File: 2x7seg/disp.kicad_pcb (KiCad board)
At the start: 2 copper layers, 35.8 x 30.5 mm, 11 parts, among them P1 CONN_01X08, P2 CONN_01X08, U1 TLC59282

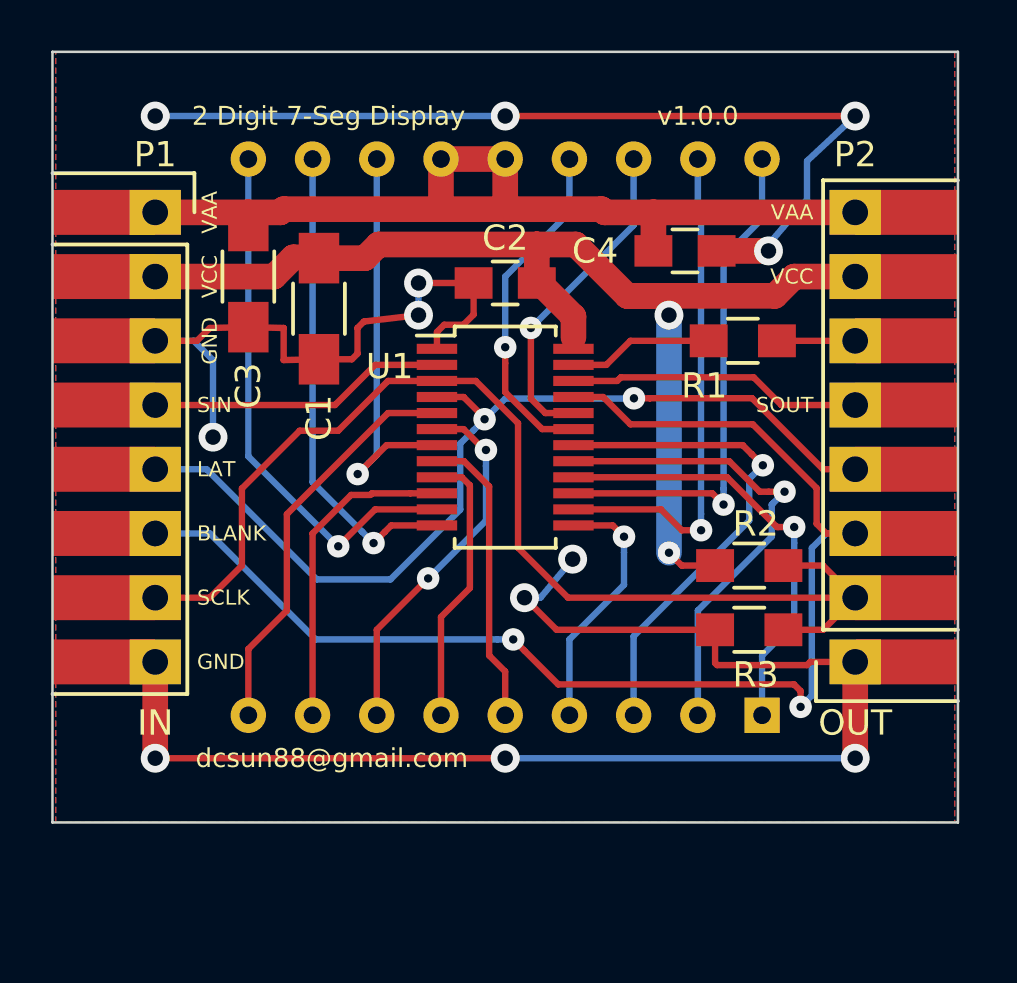
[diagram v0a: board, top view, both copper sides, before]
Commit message: Next version of display board. Increase size of holes for display pins.
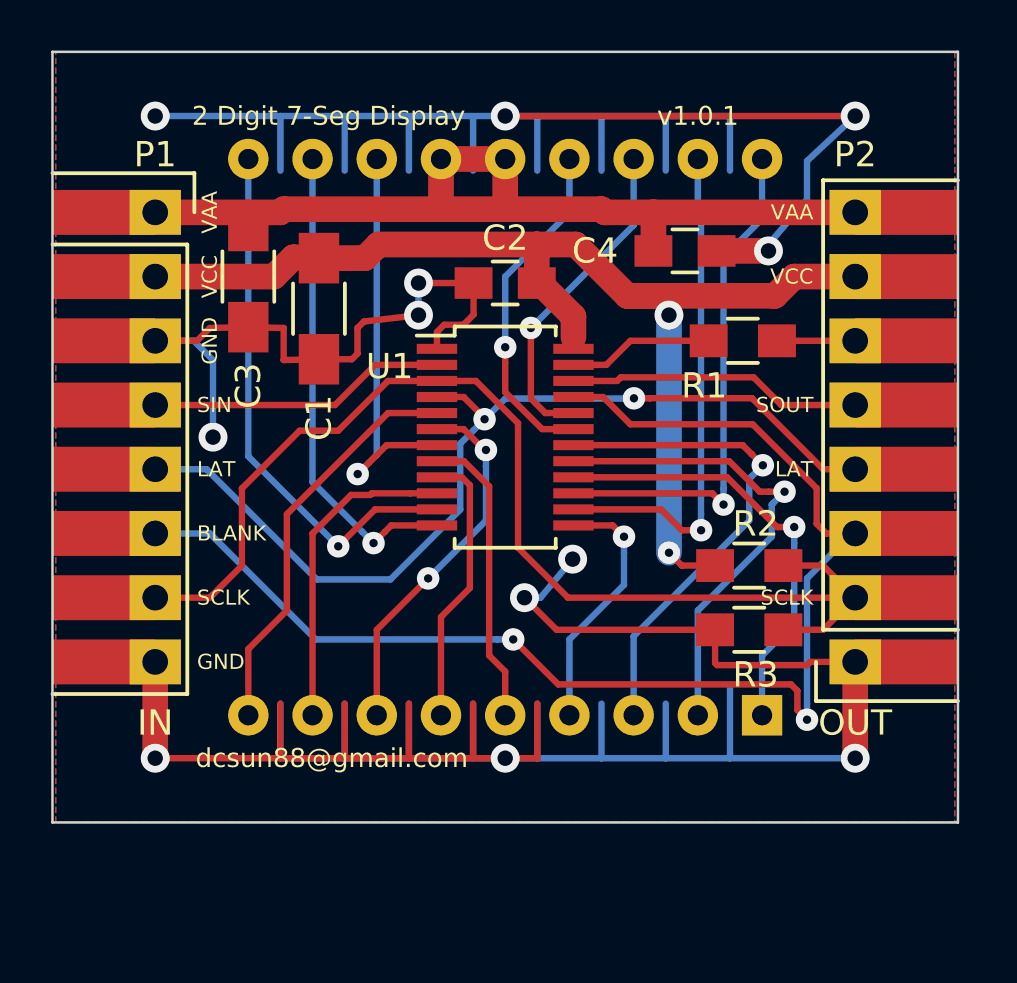
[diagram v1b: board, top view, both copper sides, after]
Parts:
- R1: value 5.05K -> 5.11K
- R2, R3: value 200 -> 249
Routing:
- net GND: track 124.6 -> 189.7 mm
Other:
- board text added: "v1.0.1"
- board text removed: "v1.0.0"

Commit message: Hide value in stitching via. Reduce width of display board by 10 mils.
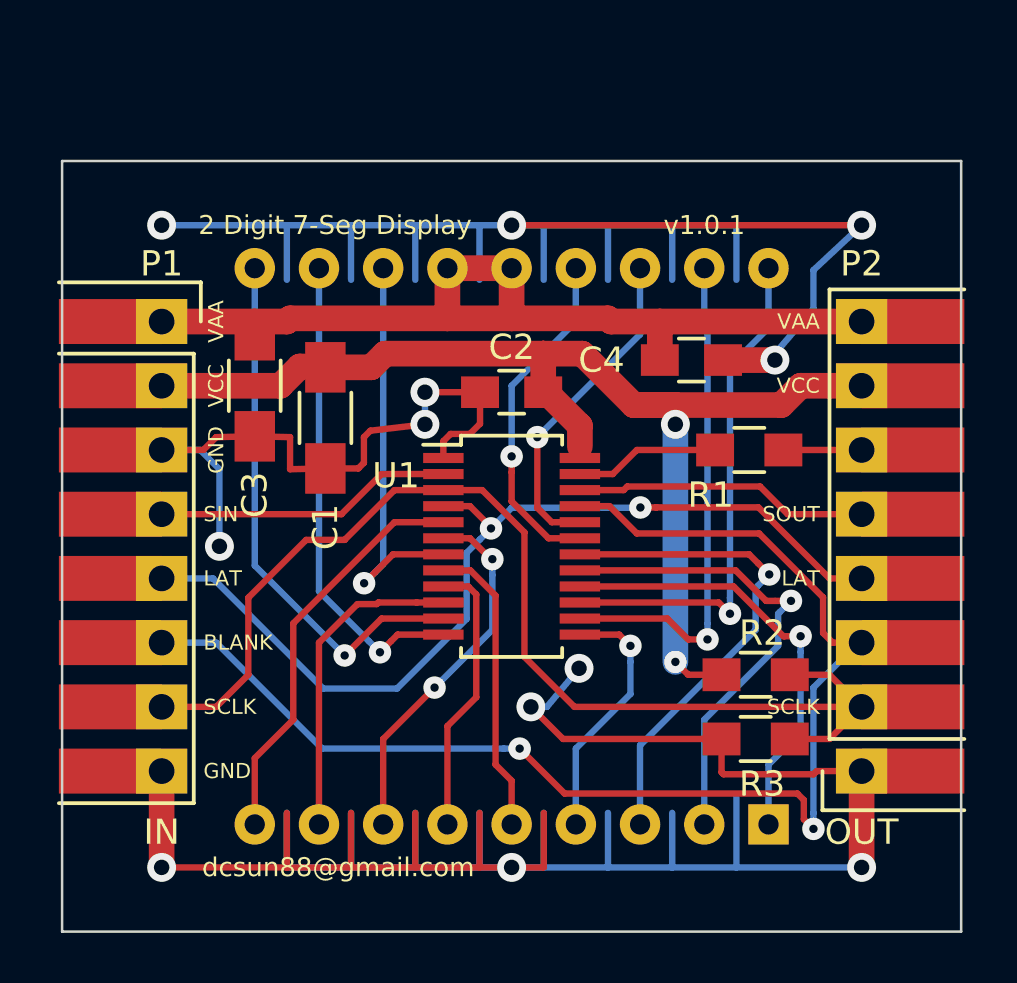
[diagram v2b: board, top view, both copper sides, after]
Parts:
- moved R3 4.33 mm to (154.4, 106.7)
- moved P1 4.33 mm to (130.9, 90.2)
- moved C1 4.33 mm to (137.4, 94.0)
- moved C2 4.33 mm to (144.8, 93.0)
- moved C3 4.33 mm to (134.6, 92.7)
- moved C4 4.33 mm to (151.9, 91.7)
- moved DS1 4.33 mm to (144.8, 99.1)
- moved P2 4.33 mm to (158.6, 108.0)
- moved R1 4.33 mm to (154.2, 95.2)
- moved R2 4.33 mm to (154.4, 104.1)
- moved U1 4.33 mm to (144.8, 99.1)
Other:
- board size 35.8 x 30.5 mm -> 35.6 x 30.5 mm

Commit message: Generate PDF schematics.
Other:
- board text added: "dcsun88osh@gmail.com"
- board text removed: "dcsun88@gmail.com"
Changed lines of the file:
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@@
     (links 63)
     (no_connects 0)
-    (area 126.949999 83.769999 162.610001 114.350001)
+    (area 125.774667 83.276 163.785334 114.694)
     (thickness 1.6)
     (drawings 24)
@@
     (effects (font (size 0.75 0.75) (thickness 0.15)))
   )
-  (gr_text dcsun88@gmail.com (at 137.922 111.76) (layer F.SilkS)
+  (gr_text dcsun88osh@gmail.com (at 139.446 111.76) (layer F.SilkS)
     (effects (font (size 0.75 0.75) (thickness 0.15)))
   )

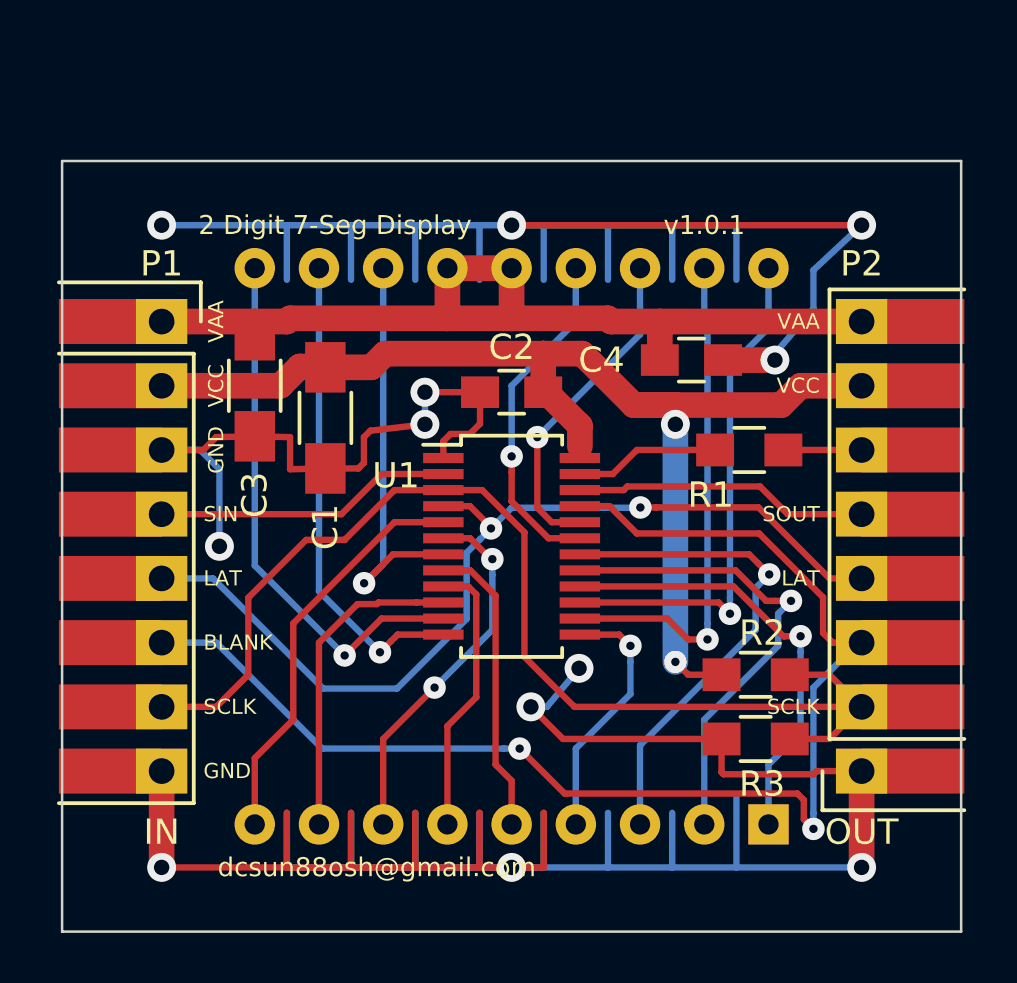
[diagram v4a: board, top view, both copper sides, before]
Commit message: Remove termination resistors on clock line.
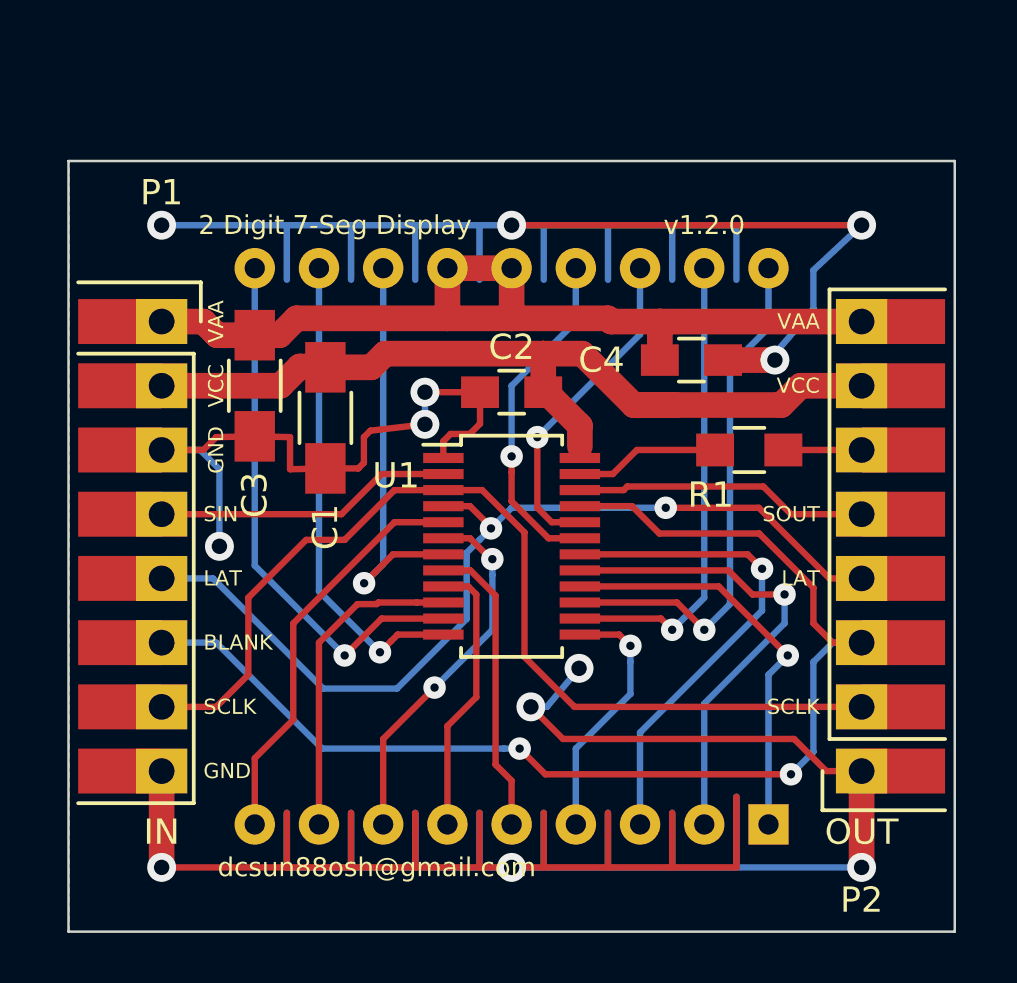
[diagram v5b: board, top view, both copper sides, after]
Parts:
- removed R2, R3: 249, Resistors_SMD:R_0805_HandSoldering
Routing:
- net GND: track 189.7 -> 203.5 mm
- net VCC: track 52.1 -> 39.9 mm, vias 2 -> 0
- net /SCLK: track 50.3 -> 43.5 mm
- net /BLANK: track 54.0 -> 50.6 mm
- net /D1g: track 20.1 -> 18.7 mm
- net /D1e: track 17.5 -> 16.4 mm
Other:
- board size 35.6 x 30.5 mm -> 35.1 x 30.5 mm
- board text added: "v1.2.0"
- board text removed: "v1.0.1"

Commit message: Change footprints for 0805 and 1206 packages.
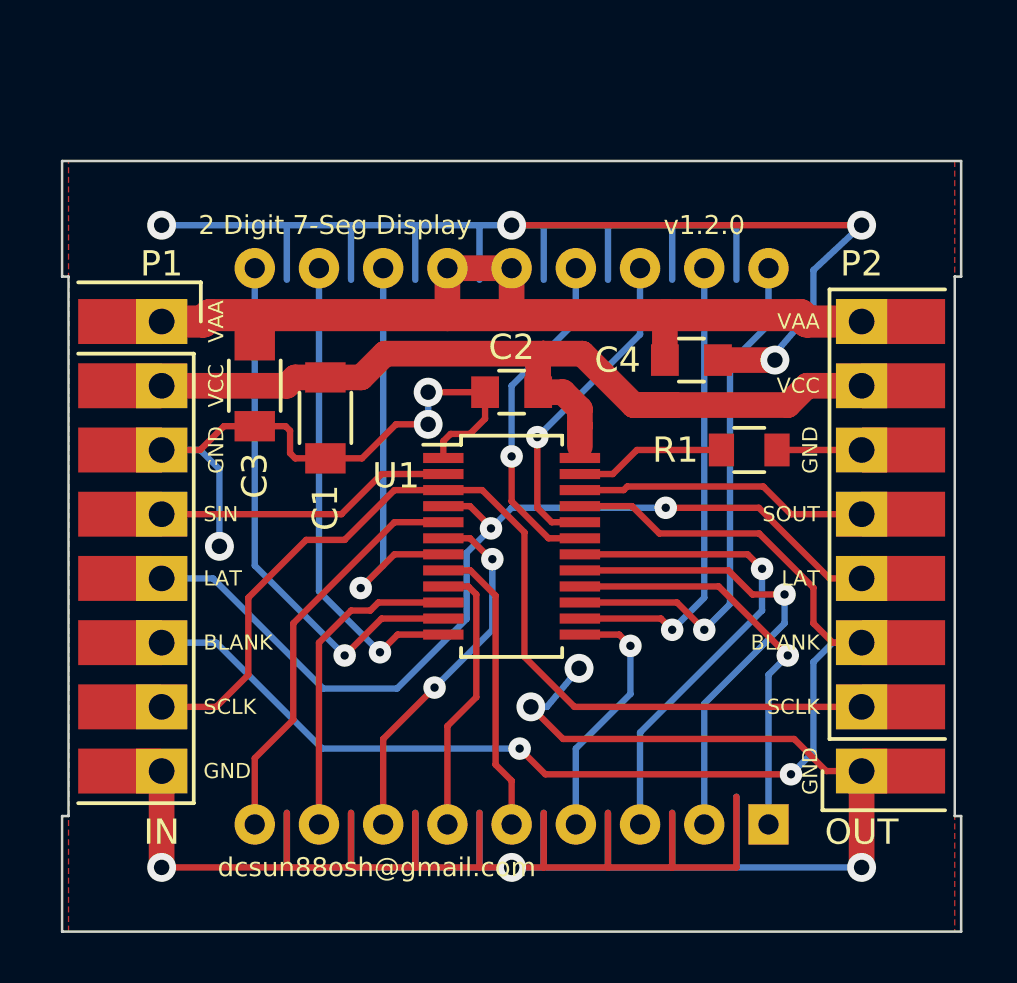
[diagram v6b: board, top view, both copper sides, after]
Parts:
- C1, C3: footprint Capacitors_SMD:C_1206_HandSoldering -> local:C_1206_HandSoldering
- C2, C4: footprint Capacitors_SMD:C_0805_HandSoldering -> local:C_0805_HandSoldering
- R1: footprint Resistors_SMD:R_0805_HandSoldering -> local:R_0805_HandSoldering
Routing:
- net VAA: track 36.3 -> 37.1 mm
- net VCC: track 39.9 -> 40.6 mm
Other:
- board size 35.1 x 30.5 mm -> 35.6 x 30.5 mm

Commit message: Generate output files for display board. Minor clean up of silkscreen and stitching vias.
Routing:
- net GND: track 203.5 -> 190.0 mm, vias 12 -> 14
- net /BLANK: track 50.6 -> 49.0 mm
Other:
- board text added: "dcsun88osh@ gmail.com"
- board text removed: "dcsun88osh@gmail.com"
